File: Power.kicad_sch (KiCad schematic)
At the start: 42 parts, among them J10 Conn_01x02_Socket, Q1 SiRA24DP, Q2 SiRA12DP, U19 MCP19035-BAABE/MF, U20 TPS7A4701xRGW, U21 MIC23201YML-TR

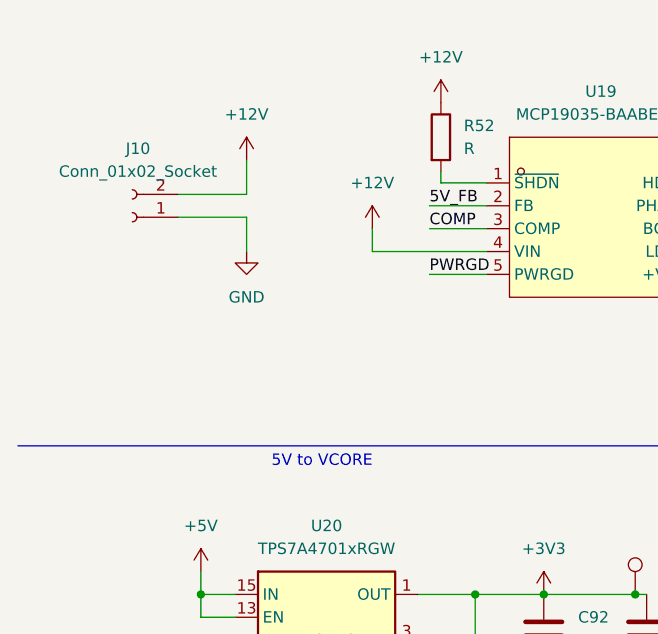
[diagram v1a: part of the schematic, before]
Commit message: TPS25762 EEPROM connector added
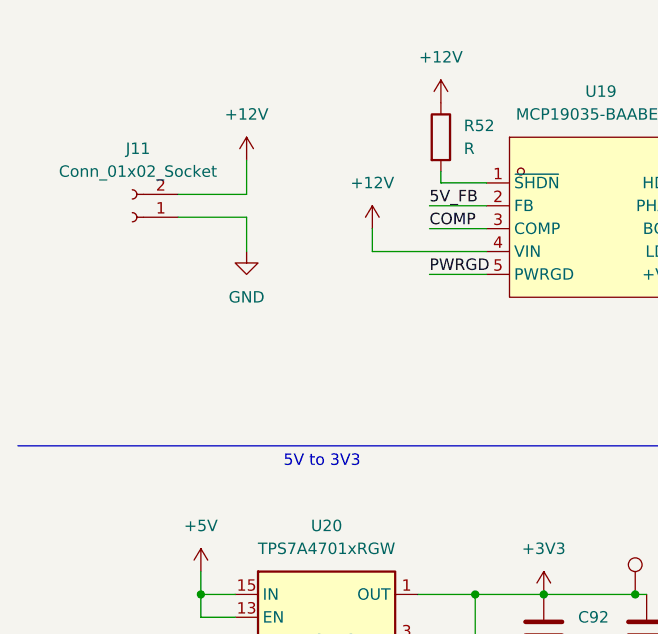
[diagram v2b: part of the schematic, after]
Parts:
- renumbered J10 to J11
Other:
- note added: "5V to 3V3"
- title: (none) -> USB Hub
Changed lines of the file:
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@@
 	(generator_version "9.0")
 	(paper "A4")
+	(title_block
+		(title "USB Hub")
+	)
 	(text "V_OUT = 1.4 + pins"
 		(exclude_from_sim no)
@@
 		)
 	)
-	(text "5V to VCORE"
+	(text "5V to 3V3"
 		(exclude_from_sim no)
 		(at 46.482 61.468 0)
@@
 		(dnp no)
 		(fields_autoplaced yes)
-		(property "Reference" "J10"
+		(property "Reference" "J11"
 			(at 26.035 26.67 0)
 			(effects
@@
 			(project ""
 				(path "/a2586c28-95f1-49e6-9254-37d7a8473e53/d2423802-44ec-4cde-beeb-19921a82a533"
-					(reference "J10")
+					(reference "J11")
 					(unit 1)
 				)

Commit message: deleted duplicated capacitor
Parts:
- removed C86: 0.33uF, symbol Device:C
- C100: renamed from C101; footprint 0.1uF -> Capacitor_SMD:C_0402_1005Metric
- C82, C83, C84, C85: footprint (none) -> Capacitor_SMD:C_0402_1005Metric
- C86: renamed from C87; footprint (none) -> Capacitor_THT:C_Radial_D10.0mm_H16.0mm_P5.00mm
- C87: renamed from C88; footprint (none) -> Capacitor_THT:C_Radial_D10.0mm_H16.0mm_P5.00mm
- C88: renamed from C89; footprint (none) -> Capacitor_THT:C_Radial_D10.0mm_H16.0mm_P5.00mm
- C89: renamed from C90; footprint (none) -> Capacitor_SMD:C_0402_1005Metric
- C90: renamed from C91; footprint (none) -> Capacitor_SMD:C_0402_1005Metric
- C91: renamed from C92; footprint (none) -> Capacitor_SMD:C_0402_1005Metric
- C92: renamed from C93; footprint (none) -> Capacitor_SMD:C_0402_1005Metric
- C93: renamed from C94; footprint (none) -> Capacitor_SMD:C_0402_1005Metric
- C94: renamed from C95; footprint (none) -> Capacitor_SMD:C_0402_1005Metric
- C95: renamed from C96; footprint 0.1uF -> Capacitor_SMD:C_0402_1005Metric
- C96: renamed from C97; footprint 0.1uF -> Capacitor_SMD:C_0402_1005Metric
- C97: renamed from C98; footprint (none) -> Capacitor_SMD:C_0402_1005Metric
- C98: renamed from C99; footprint (none) -> Capacitor_SMD:C_0402_1005Metric
- C99: renamed from C100; footprint 0.1uF -> Capacitor_SMD:C_0402_1005Metric
- D6: footprint (none) -> Diode_SMD:D_SMB
- J11: footprint (none) -> Connector_PinHeader_1.27mm:PinHeader_1x02_P1.27mm_Vertical
- L2, L3: footprint (none) -> Inductor_SMD:L_6.3x6.3_H3
- Q1, Q2: footprint (none) -> Package_SO:PowerPAK_SO-8_Single
- R52, R53, R54, R55, R56, R57, R58, R59, R60, R61: footprint (none) -> Resistor_SMD:R_0603_1608Metric
- TP7, TP8, TP9: footprint (none) -> TestPoint:TestPoint_THTPad_1.5x1.5mm_Drill0.7mm
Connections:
- net +12V: now also Q1.5 (D), Q1.6 (D), Q1.7 (D), Q1.8 (D); no longer Q1.1 (D)
- net GND: now also Q2.1 (S), Q2.2 (S)
- net HDRV: now also Q1.4 (G); no longer Q1.2 (G)
- net LDRV: now also Q2.4 (G); no longer Q2.2 (G)
- net PHASE: now also Q1.1 (S), Q1.2 (S), Q2.5 (D), Q2.6 (D), Q2.7 (D), Q2.8 (D); no longer Q2.1 (D)

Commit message: Minor fixes
Fixed unclear labelling of buses
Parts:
- R52, R53, R54, R55, R56, R57, R58, R59, R60, R61: footprint Resistor_SMD:R_0603_1608Metric -> Resistor_SMD:R_0402_1005Metric
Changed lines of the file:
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@@
 			)
 		)
-		(property "Footprint" "Resistor_SMD:R_0603_1608Metric"
+		(property "Footprint" "Resistor_SMD:R_0402_1005Metric"
 			(at 242.062 27.94 90)
 			(effects
@@
 			)
 		)
-		(property "Footprint" "Resistor_SMD:R_0603_1608Metric"
+		(property "Footprint" "Resistor_SMD:R_0402_1005Metric"
 			(at 115.062 181.61 90)
 			(effects
@@
 			)
 		)
-		(property "Footprint" "Resistor_SMD:R_0603_1608Metric"
+		(property "Footprint" "Resistor_SMD:R_0402_1005Metric"
 			(at 67.31 173.228 90)
 			(effects
@@
 			)
 		)
-		(property "Footprint" "Resistor_SMD:R_0603_1608Metric"
+		(property "Footprint" "Resistor_SMD:R_0402_1005Metric"
 			(at 106.68 42.418 90)
 			(effects
@@
 			)
 		)
-		(property "Footprint" "Resistor_SMD:R_0603_1608Metric"
+		(property "Footprint" "Resistor_SMD:R_0402_1005Metric"
 			(at 273.05 31.242 90)
 			(effects
@@
 			)
 		)
-		(property "Footprint" "Resistor_SMD:R_0603_1608Metric"
+		(property "Footprint" "Resistor_SMD:R_0402_1005Metric"
 			(at 57.912 25.4 90)
 			(effects
@@
 			)
 		)
-		(property "Footprint" "Resistor_SMD:R_0603_1608Metric"
+		(property "Footprint" "Resistor_SMD:R_0402_1005Metric"
 			(at 250.698 38.1 90)
 			(effects
@@
 			)
 		)
-		(property "Footprint" "Resistor_SMD:R_0603_1608Metric"
+		(property "Footprint" "Resistor_SMD:R_0402_1005Metric"
 			(at 96.52 185.928 90)
 			(effects
@@
 			)
 		)
-		(property "Footprint" "Resistor_SMD:R_0603_1608Metric"
+		(property "Footprint" "Resistor_SMD:R_0402_1005Metric"
 			(at 115.062 171.45 90)
 			(effects
@@
 			)
 		)
-		(property "Footprint" "Resistor_SMD:R_0603_1608Metric"
+		(property "Footprint" "Resistor_SMD:R_0402_1005Metric"
 			(at 261.62 29.718 90)
 			(effects

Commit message: Scheme fixes
Fixed wrong connection of SNS pin of U21
USB7206c symbol improved
R7's value fixed
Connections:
- net VCORE: now also U21.3 (SNS)
- net at L3.1, U21.1 (SW): no longer U21.3 (SNS)
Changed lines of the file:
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@@
+	)
+	(junction
+		(at 114.3 165.1)
+		(diameter 0)
+		(color 0 0 0 0)
 	)
 	(junction
@@
 	(junction
 		(at 243.84 33.02)
-		(diameter 0)
-		(color 0 0 0 0)
-	)
-	(junction
-		(at 102.87 165.1)
 		(diameter 0)
 		(color 0 0 0 0)
@@
 	(wire
 		(pts
-			(xy 102.87 165.1) (xy 105.41 165.1)
-		)
-		(stroke
-			(width 0)
-			(type default)
-		)
-	)
-	(wire
-		(pts
 			(xy 50.8 165.1) (xy 50.8 167.64)
 		)
@@
 	(wire
 		(pts
-			(xy 92.71 165.1) (xy 102.87 165.1)
+			(xy 92.71 165.1) (xy 105.41 165.1)
 		)
 		(stroke
@@
 	(wire
 		(pts
+			(xy 114.3 167.64) (xy 114.3 165.1)
+		)
+		(stroke
+			(width 0)
+			(type default)
+		)
+	)
+	(wire
+		(pts
 			(xy 193.04 43.18) (xy 203.2 43.18)
 		)
@@
 	(wire
 		(pts
-			(xy 102.87 167.64) (xy 102.87 165.1)
-		)
-		(stroke
-			(width 0)
-			(type default)
-		)
-	)
-	(wire
-		(pts
 			(xy 238.76 24.13) (xy 243.84 24.13)
 		)
@@
 	(wire
 		(pts
+			(xy 114.3 165.1) (xy 116.84 165.1)
+		)
+		(stroke
+			(width 0)
+			(type default)
+		)
+	)
+	(wire
+		(pts
 			(xy 29.21 93.98) (xy 36.83 93.98)
 		)
@@
 	(wire
 		(pts
-			(xy 113.03 165.1) (xy 116.84 165.1)
+			(xy 113.03 165.1) (xy 114.3 165.1)
 		)
 		(stroke
@@
 	(wire
 		(pts
-			(xy 92.71 167.64) (xy 102.87 167.64)
-		)
-		(stroke
+			(xy 92.71 167.64) (xy 114.3 167.64)
+		)
+		(stroke

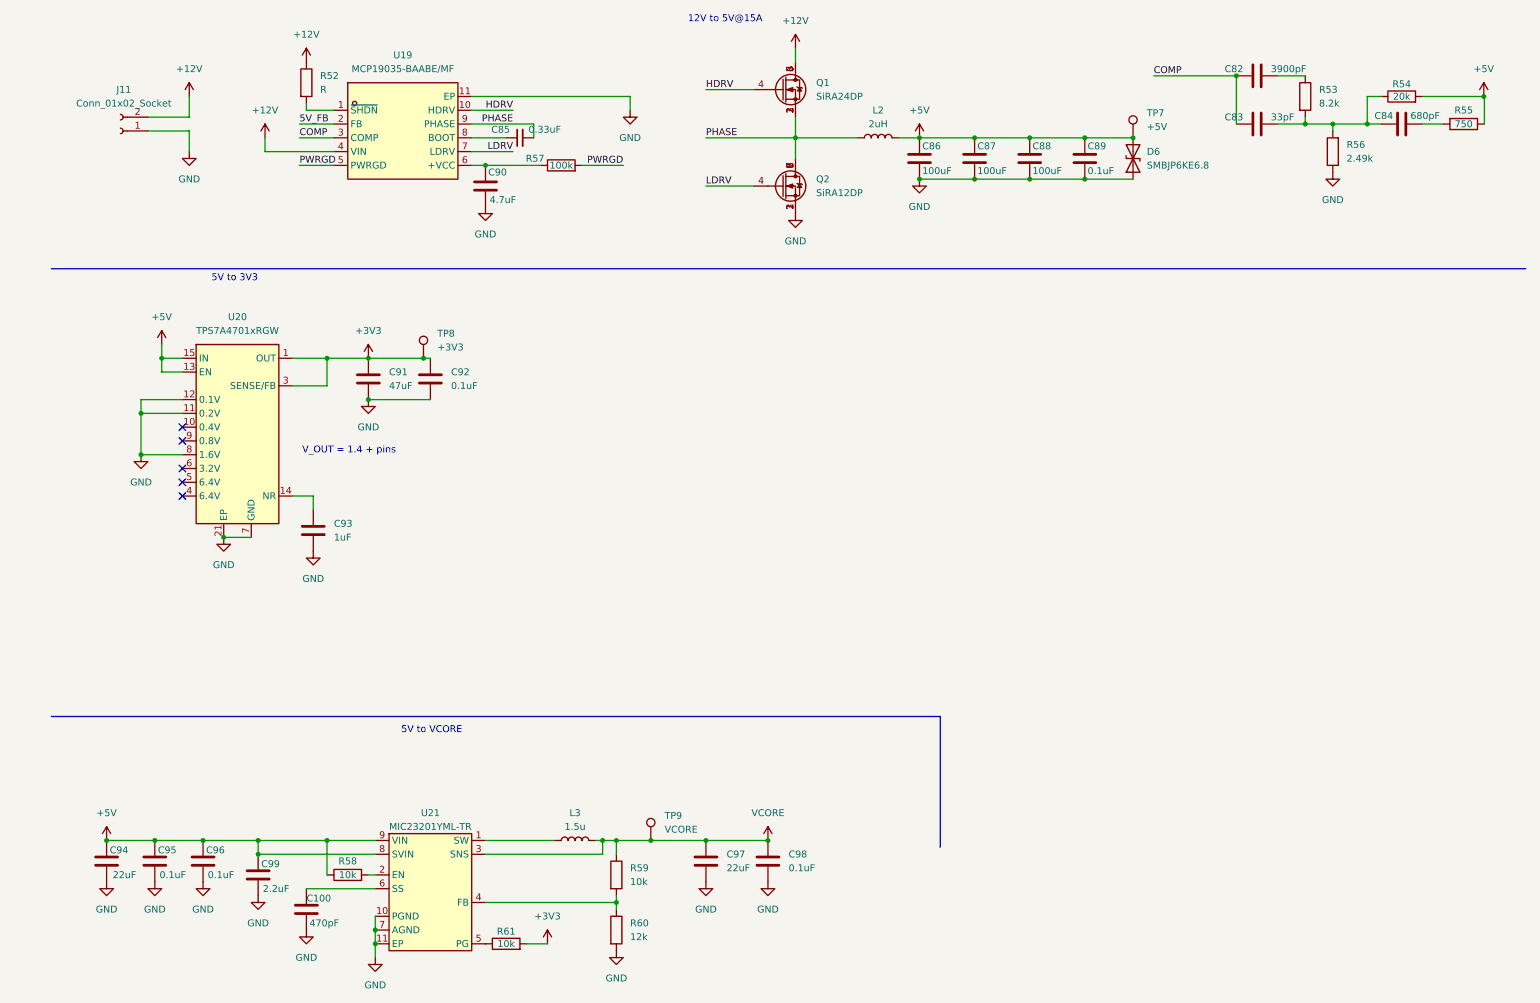
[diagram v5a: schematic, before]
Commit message: MCP19035 changed to MP8795
TPS7A4701xRGW to AP7361C-33E
Led Indicator added
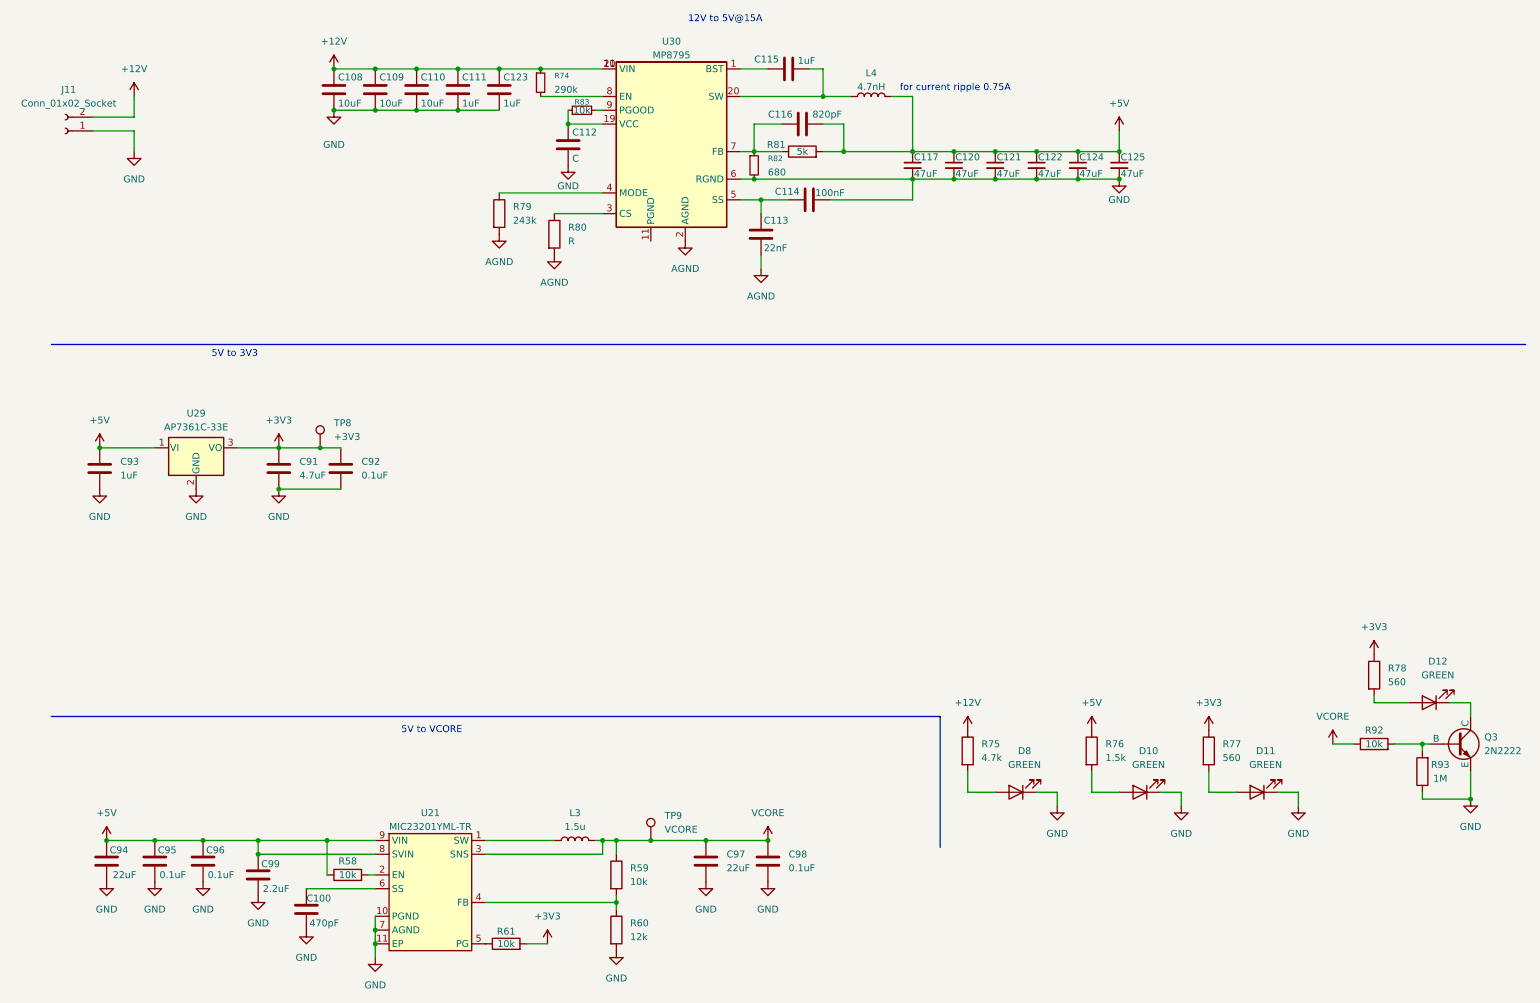
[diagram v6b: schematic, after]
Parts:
- removed C82: 3900pF, Capacitor_SMD:C_0402_1005Metric, symbol Device:C
- removed C83: 33pF, Capacitor_SMD:C_0402_1005Metric, symbol Device:C
- removed C84: 680pF, Capacitor_SMD:C_0402_1005Metric, symbol Device:C
- removed C85: 0.33uF, Capacitor_SMD:C_0402_1005Metric, symbol Device:C_Small
- removed C86, C87, C88: 100uF, Capacitor_THT:C_Radial_D10.0mm_H16.0mm_P5.00mm, symbol Device:C
- removed C89: 0.1uF, Capacitor_SMD:C_0402_1005Metric, symbol Device:C
- removed C90: 4.7uF, Capacitor_SMD:C_0402_1005Metric, symbol Device:C
- removed D6: SMBJP6KE6.8, Diode_SMD:D_SMB, symbol Device:D_TVS
- removed L2: 2uH, Inductor_SMD:L_6.3x6.3_H3, symbol Device:L
- removed Q1: SiRA24DP, Package_SO:PowerPAK_SO-8_Single, symbol Transistor_FET_Other:Q_NMOS_Depletion_DGS
- removed Q2: SiRA12DP, Package_SO:PowerPAK_SO-8_Single, symbol Transistor_FET_Other:Q_NMOS_Depletion_DGS
- removed R52: R, Resistor_SMD:R_0402_1005Metric, symbol Device:R
- removed R53: 8.2k, Resistor_SMD:R_0402_1005Metric, symbol Device:R
- removed R54: 20k, Resistor_SMD:R_0402_1005Metric, symbol Device:R
- removed R55: 750, Resistor_SMD:R_0402_1005Metric, symbol Device:R
- removed R56: 2.49k, Resistor_SMD:R_0402_1005Metric, symbol Device:R
- removed R57: 100k, Resistor_SMD:R_0402_1005Metric, symbol Device:R
- removed TP7: +5V, TestPoint:TestPoint_THTPad_1.5x1.5mm_Drill0.7mm, symbol Connector:TestPoint
- removed U19: MCP19035-BAABE/MF, EasyEDA:DFN-10_L3.0-W3.0-P0.50-BL-EP-1, symbol EasyEDA:MCP19035-BAABE_MF
- removed U20: TPS7A4701xRGW, Package_DFN_QFN:Texas_RGW0020A_VQFN-20-1EP_5x5mm_P0.65mm_EP3.15x3.15mm_ThermalVias, symbol Regulator_Linear:TPS7A4701xRGW
- added C108, C109, C110: 10uF, symbol Device:C
- added C111, C115, C123: 1uF, symbol Device:C
- added C112: C, symbol Device:C
- added C113: 22nF, symbol Device:C
- added C114: 100nF, symbol Device:C
- added C116: 820pF, symbol Device:C
- added C117, C120, C121, C122, C124, C125: 47uF, symbol Device:C_Small
- added D10, D11, D12, D8: GREEN, symbol Device:LED
- added L4: 4.7nH, symbol Device:L
- added Q3: 2N2222, symbol Simulation_SPICE:NPN
- added R74: 290k, symbol Device:R_Small
- added R75: 4.7k, symbol Device:R
- added R76: 1.5k, symbol Device:R
- added R77, R78: 560, symbol Device:R
- added R79: 243k, symbol Device:R
- added R80: R, symbol Device:R
- added R81: 5k, symbol Device:R
- added R82: 680, symbol Device:R_Small
- added R83: 10k, symbol Device:R_Small
- added R92: 10k, symbol Device:R
- added R93: 1M, symbol Device:R
- added U29: AP7361C-33E, Package_TO_SOT_SMD:SOT-223-3_TabPin2, symbol Regulator_Linear:AP7361C-33E
- added U30: MP8795, symbol Snapeda:MP8795
- C91: value 47uF -> 4.7uF
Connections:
- net +12V: now also C108.1, C109.1, C110.1, C111.1, C123.1, R74.1, R75.1, U30.10 (VIN), U30.21 (VIN)
- net +3V3: now also R77.1, R78.1, U29.3 (VO)
- net +5V: now also C93.1, C116.2, C117.1, C120.1, C121.1, C122.1, C124.1, C125.1, L4.2, R76.1, R81.2, U29.1 (VI)
- net GND: now also C108.2, C109.2, C110.2, C111.2, C112.2, C114.2, C117.2, C120.2, C121.2, C122.2, C123.2, C124.2, C125.2, D10.1 (K), D11.1 (K), D8.1 (K), Q3.3 (E), R82.2, R93.1, U29.2 (GND), U30.6 (RGND)
- net VCORE: now also R92.1
- new net: C113.1, C114.1, U30.5 (SS)
- new net: D8.2 (A), R75.2
- new net: C116.1, R81.1, R82.1, U30.7 (FB)
- new net: Q3.2 (B), R92.2, R93.2
- new net: R74.2, U30.8 (EN)
- new net: R79.1, U30.4 (MODE)
- new net: D10.2 (A), R76.2
- new net: D12.2 (A), R78.2
- new net: R80.1, U30.3 (CS)
- new net: D11.2 (A), R77.2
- new net: C115.1, U30.1 (BST)
- new net: C115.2, L4.1, U30.20 (SW)
- new net: D12.1 (K), Q3.1 (C)
- new net: C112.1, R83.1, U30.19 (VCC)
- new net: R83.2, U30.9 (PGOOD)
- new net AGND: C113.2, R79.2, R80.2, U30.2 (AGND)
- no-connect marks 5 -> 0
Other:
- note added: "for current ripple 0.75A"
- note removed: "V_OUT = 1.4 + pins"
- moved on the sheet: C91, C92, C93, J11, TP8
